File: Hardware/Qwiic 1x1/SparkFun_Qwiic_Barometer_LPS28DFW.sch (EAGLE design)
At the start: 26 parts, among them J1 QWIIC_RIGHT_ANGLE, J2 QWIIC_RIGHT_ANGLE, U1 LPS28DFW

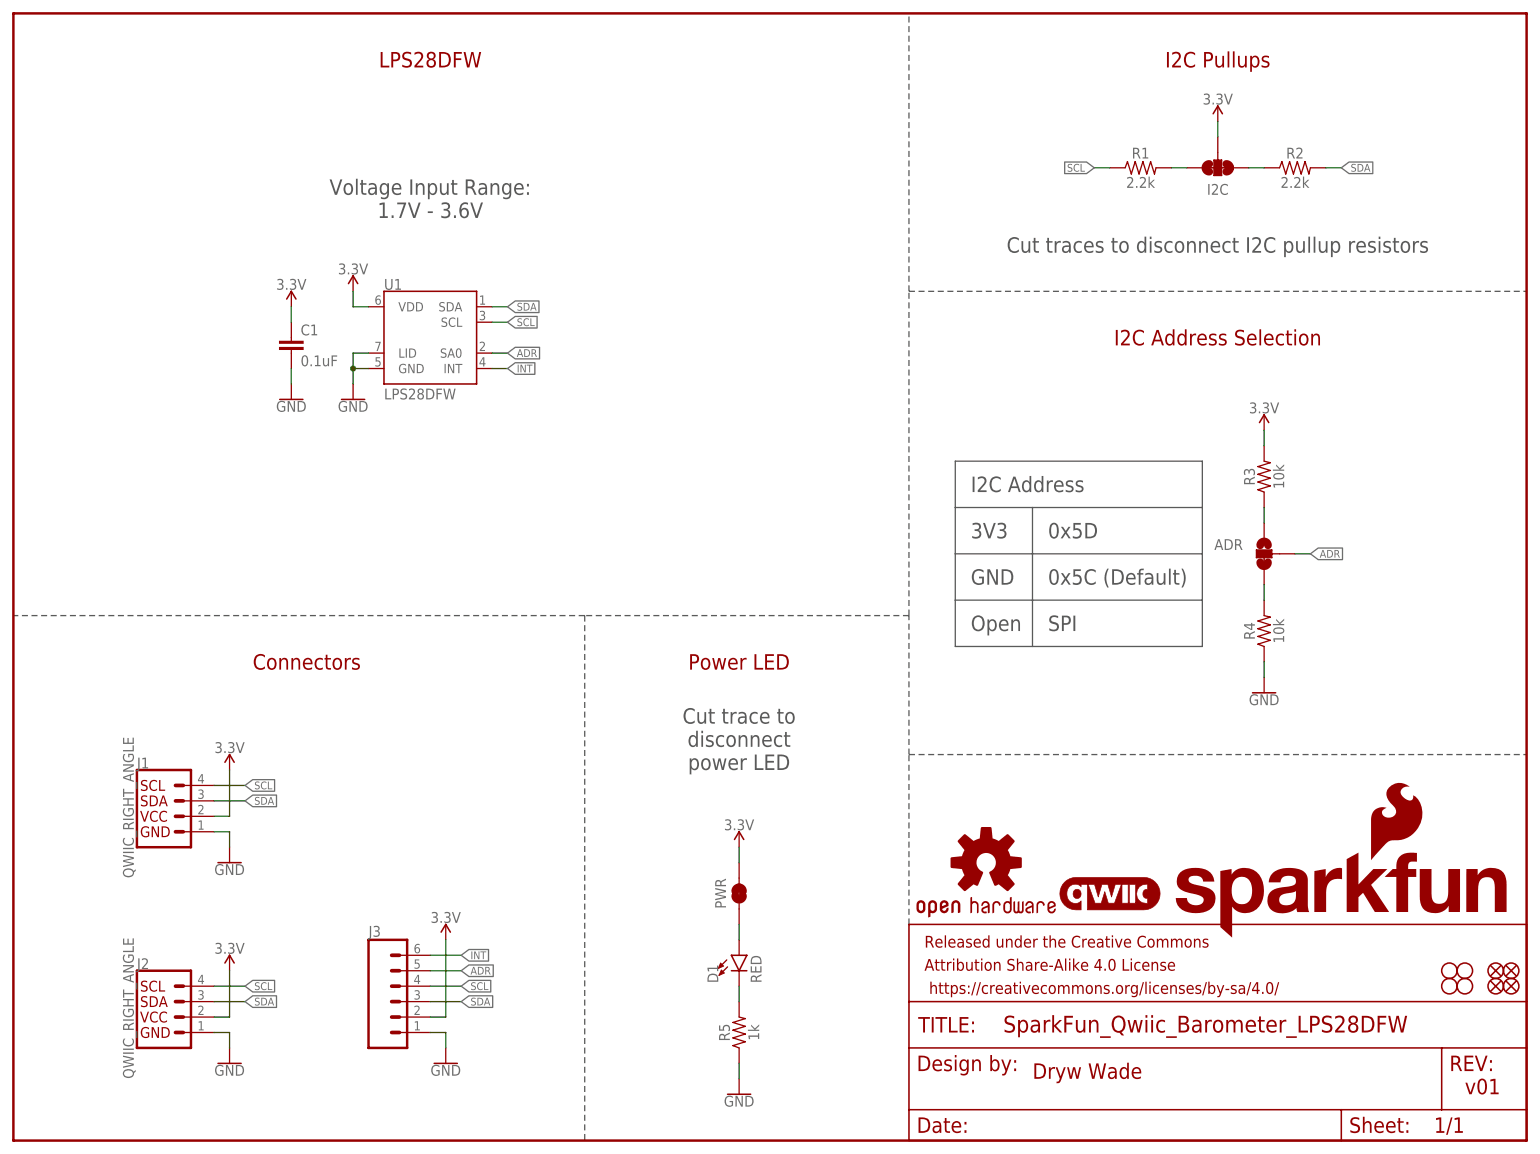
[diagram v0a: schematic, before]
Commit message: Design review updates
Both:
Bump version number to v10
Change LPS28DF section name to "Barometer - LPS28DFW" in schematics
Remove SPI from ADR jumper in schematics
Add ordering instructions to boards

1x1:
Make SCL and SDA traces not overlap near Qwiic connector
Move OSHW down between connector and standoff
Move I@C jumper up to give more GND pour under sensor
Add SparkFun logo to bottom silk

Micro:
Space out test points in schematic
Add text about 22 AWG wires in schematic
Move OSHW logo up slightly to not clip at test points
Flip ADR labels to be correct
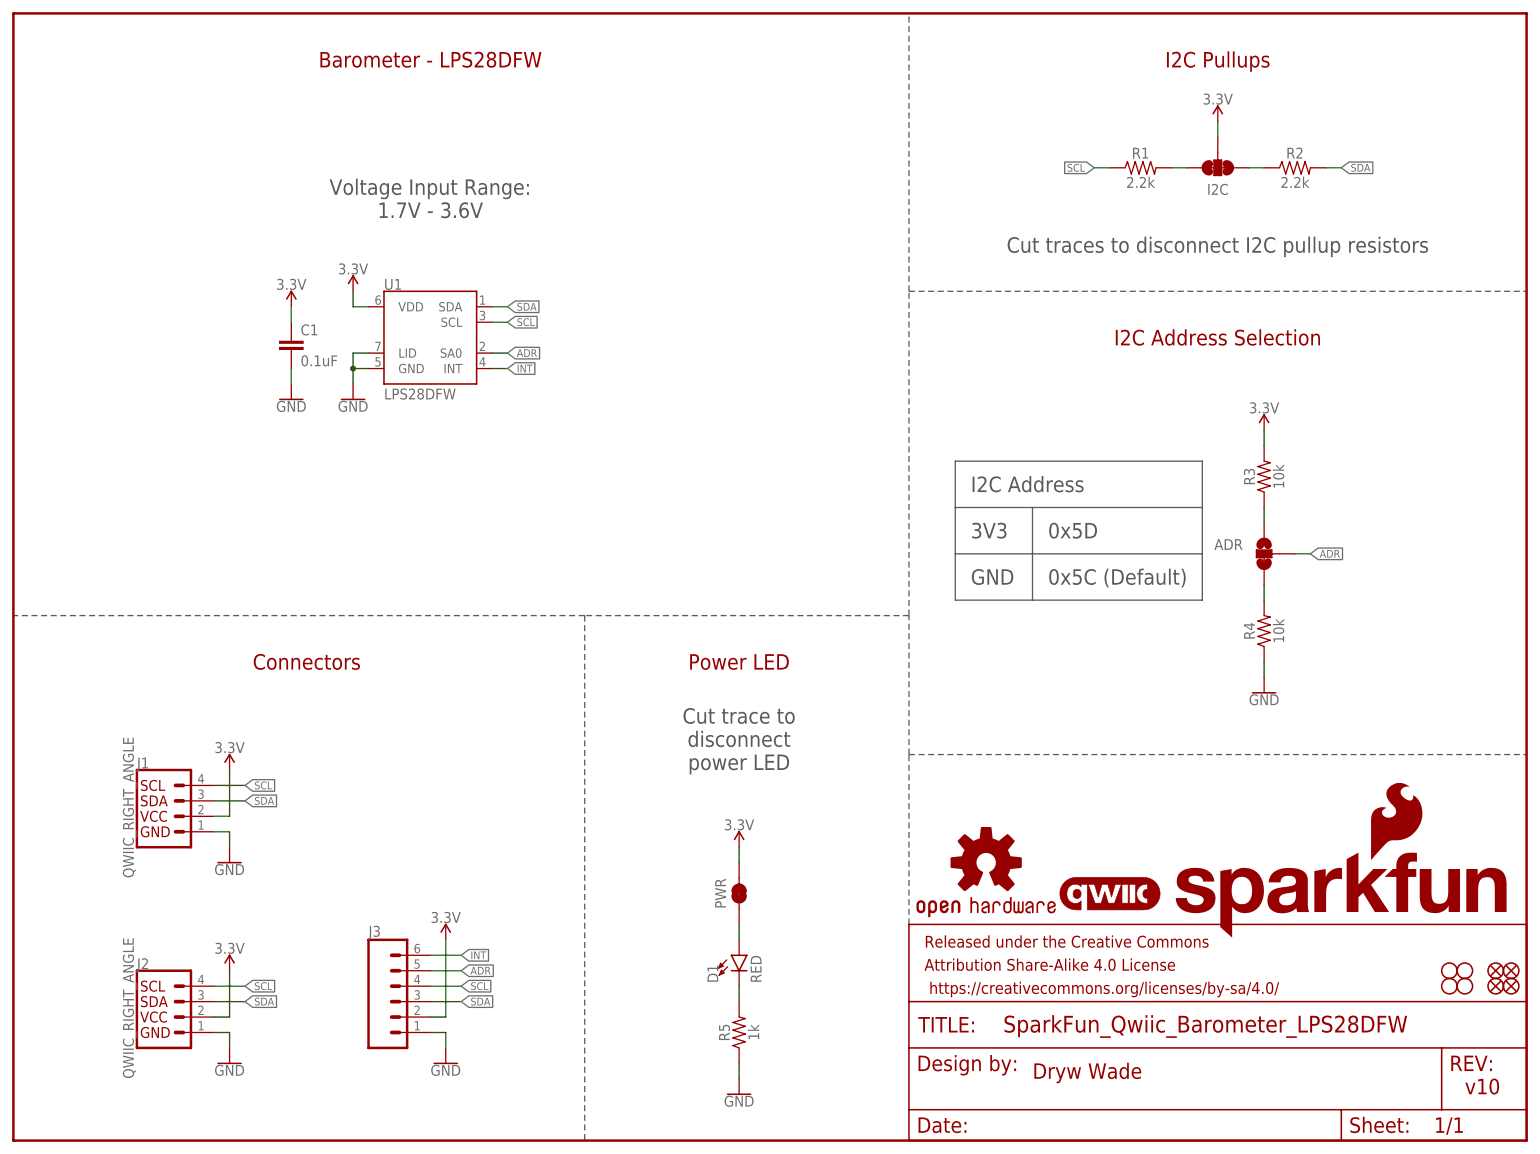
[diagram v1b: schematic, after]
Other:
- note added: "Barometer - LPS28DFW"
- note added: "v10"
- note removed: "LPS28DFW"
- note removed: "Open"
- note removed: "SPI"
- note removed: "v01"
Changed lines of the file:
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@@
 <plain>
 <text x="167.64" y="10.16" size="2.54" layer="94" font="vector">Dryw Wade</text>
-<text x="238.76" y="7.62" size="2.54" layer="94" font="vector">v01</text>
-<text x="68.58" y="177.8" size="2.54" layer="94" font="vector" align="center">LPS28DFW</text>
+<text x="238.76" y="7.62" size="2.54" layer="94" font="vector">v10</text>
+<text x="68.58" y="177.8" size="2.54" layer="94" font="vector" align="center">Barometer - LPS28DFW</text>
 <text x="198.12" y="177.8" size="2.54" layer="94" font="vector" align="center">I2C Pullups</text>
 <text x="198.12" y="132.08" size="2.54" layer="94" font="vector" align="center">I2C Address Selection</text>
@@
 <text x="157.48" y="91.44" size="2.54" layer="97" font="vector">GND</text>
 <text x="157.48" y="99.06" size="2.54" layer="97" font="vector">3V3</text>
-<text x="157.48" y="83.82" size="2.54" layer="97" font="vector">Open</text>
 <text x="170.18" y="99.06" size="2.54" layer="97" font="vector">0x5D</text>
 <text x="170.18" y="91.44" size="2.54" layer="97" font="vector">0x5C (Default)</text>
-<text x="170.18" y="83.82" size="2.54" layer="97" font="vector">SPI</text>
 <wire x1="154.94" y1="111.76" x2="195.58" y2="111.76" width="0.2032" layer="97"/>
 <wire x1="195.58" y1="111.76" x2="195.58" y2="104.14" width="0.2032" layer="97"/>
 <wire x1="195.58" y1="104.14" x2="195.58" y2="96.52" width="0.2032" layer="97"/>
 <wire x1="195.58" y1="96.52" x2="195.58" y2="88.9" width="0.2032" layer="97"/>
-<wire x1="195.58" y1="88.9" x2="195.58" y2="81.28" width="0.2032" layer="97"/>
-<wire x1="195.58" y1="81.28" x2="167.64" y2="81.28" width="0.2032" layer="97"/>
-<wire x1="167.64" y1="81.28" x2="154.94" y2="81.28" width="0.2032" layer="97"/>
-<wire x1="154.94" y1="81.28" x2="154.94" y2="88.9" width="0.2032" layer="97"/>
 <wire x1="154.94" y1="88.9" x2="154.94" y2="96.52" width="0.2032" layer="97"/>
 <wire x1="154.94" y1="96.52" x2="154.94" y2="104.14" width="0.2032" layer="97"/>
@@
 <wire x1="167.64" y1="104.14" x2="195.58" y2="104.14" width="0.2032" layer="97"/>
 <wire x1="154.94" y1="96.52" x2="195.58" y2="96.52" width="0.2032" layer="97"/>
-<wire x1="154.94" y1="88.9" x2="195.58" y2="88.9" width="0.2032" layer="97"/>
-<wire x1="167.64" y1="81.28" x2="167.64" y2="104.14" width="0.2032" layer="97"/>
+<wire x1="154.94" y1="88.9" x2="167.64" y2="88.9" width="0.2032" layer="97"/>
+<wire x1="167.64" y1="88.9" x2="195.58" y2="88.9" width="0.2032" layer="97"/>
+<wire x1="167.64" y1="88.9" x2="167.64" y2="104.14" width="0.2032" layer="97"/>
 <text x="119.38" y="66.04" size="2.54" layer="97" font="vector" align="center">Cut trace to
 disconnect

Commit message: Remove library file
Part is in SFE Eagle library, update part in design
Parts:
- U1: device LPS28DFW:LPS28DFW -> SparkFun-Sensors:LPS28DFW
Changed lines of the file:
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@@
 <parts>
 <part name="FRAME1" library="SparkFun-Aesthetics" deviceset="FRAME-LETTER" device=""/>
-<part name="U1" library="LPS28DFW" deviceset="LPS28DFW" device=""/>
+<part name="U1" library="SparkFun-Sensors" deviceset="LPS28DFW" device=""/>
 <part name="FD1" library="SparkFun-Aesthetics" deviceset="FIDUCIAL" device="1X2"/>
 <part name="FD2" library="SparkFun-Aesthetics" deviceset="FIDUCIAL" device="1X2"/>
